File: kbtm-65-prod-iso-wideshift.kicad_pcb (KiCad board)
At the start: 2 copper layers, 302.2 x 93.5 mm, 170 parts, among them J1 TYPE-C-31-M12_13_EDITED, J2 AVR-ISP-6, SW1 SW_Push, U1 ATmega32U4-AU, U2 WE-TVS-82400102, Y1 Crystal_GND24_Small

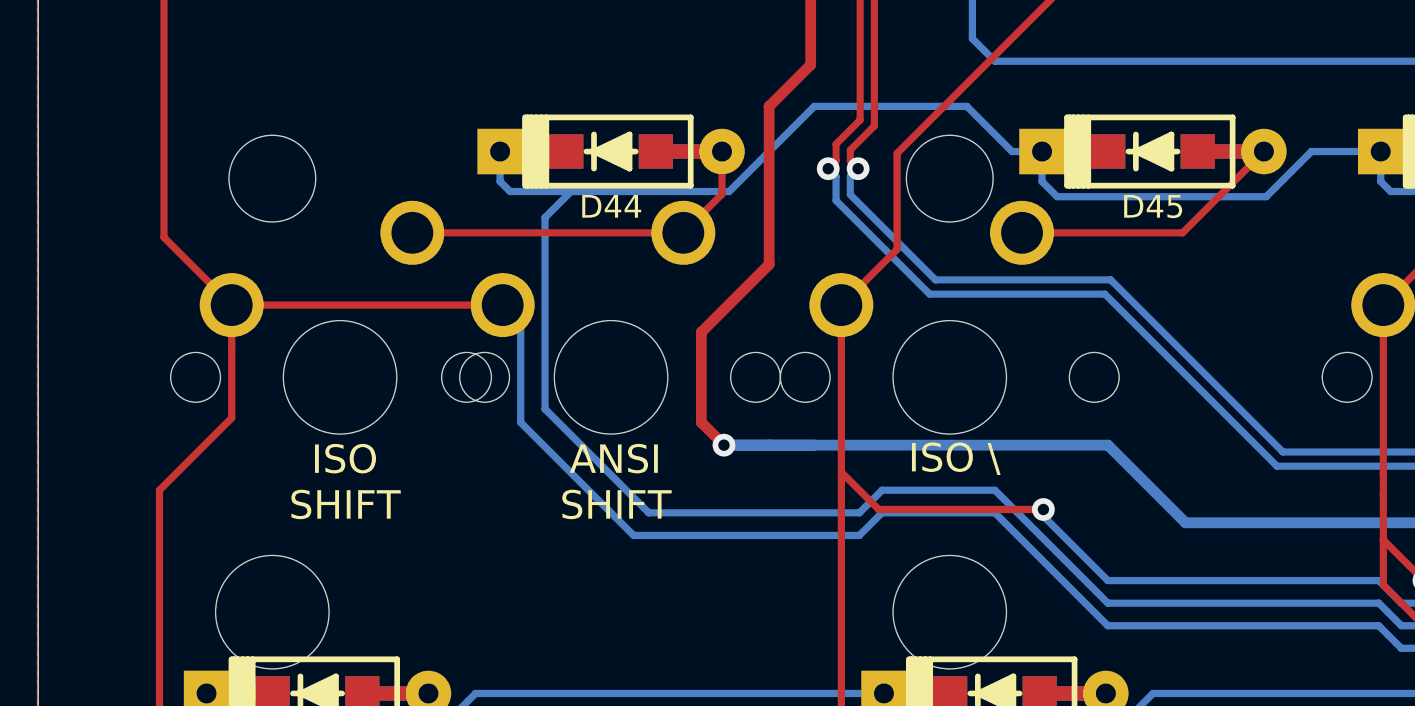
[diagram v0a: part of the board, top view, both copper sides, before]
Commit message: final prod version with all keys and fills filled in
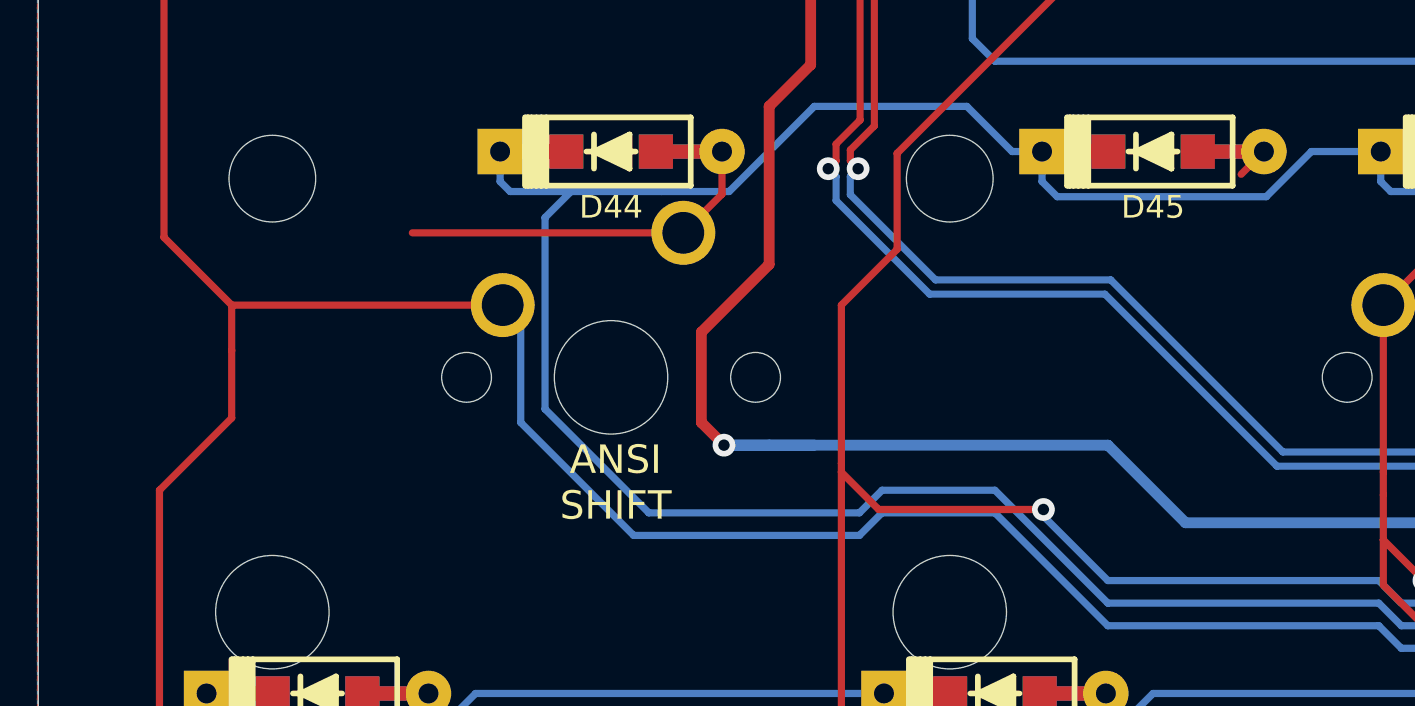
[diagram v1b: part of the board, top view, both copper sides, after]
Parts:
- removed MX_1.25U_L_SHIFT1: MX-NoLED, mini-MX-Tweaks:MXOnly-1.25U-NoLED_tweak
- removed MX_L_BSLASH1: MX-NoLED, mini-MX-Tweaks:MXOnly-1U-NoLED_tweak
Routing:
- net Net-(D45-Pad2): track 9.69 -> 1.13 mm
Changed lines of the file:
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@@
   )
   (footprint "mini-MX-Tweaks:MXOnly-1.25U-NoLED_tweak" (layer "F.Cu")
-    (at 24.60625 81.75625)
-    (attr through_hole)
-    (fp_text reference "MX_1.25U_L_SHIFT1" (at 0 3.175) (layer "Dwgs.User")
-        (effects (font (size 1 1) (thickness 0.15)))
-    )
-    (fp_text value "MX-NoLED" (at 0 -7.9375) (layer "Dwgs.User")
-        (effects (font (size 1 1) (thickness 0.15)))
-    )
-    (fp_line (start -11.90625 -9.525) (end 11.90625 -9.525)
-      (stroke (width 0.15) (type solid)) (layer "Dwgs.User"))
-    (fp_line (start -11.90625 9.525) (end -11.90625 -9.525)
-      (stroke (width 0.15) (type solid)) (layer "Dwgs.User"))
-    (fp_line (start -11.90625 9.525) (end 11.90625 9.525)
-      (stroke (width 0.15) (type solid)) (layer "Dwgs.User"))
-    (fp_line (start -7 -7) (end -7 -5)
-      (stroke (width 0.15) (type solid)) (layer "Dwgs.User"))
-    (fp_line (start -7 5) (end -7 7)
-      (stroke (width 0.15) (type solid)) (layer "Dwgs.User"))
-    (fp_line (start -7 7) (end -5 7)
-      (stroke (width 0.15) (type solid)) (layer "Dwgs.User"))
-    (fp_line (start -5 -7) (end -7 -7)
-      (stroke (width 0.15) (type solid)) (layer "Dwgs.User"))
-    (fp_line (start 5 -7) (end 7 -7)
-      (stroke (width 0.15) (type solid)) (layer "Dwgs.User"))
-    (fp_line (start 5 7) (end 7 7)
-      (stroke (width 0.15) (type solid)) (layer "Dwgs.User"))
-    (fp_line (start 7 -7) (end 7 -5)
-      (stroke (width 0.15) (type solid)) (layer "Dwgs.User"))
-    (fp_line (start 7 7) (end 7 5)
-      (stroke (width 0.15) (type solid)) (layer "Dwgs.User"))
-    (fp_line (start 11.90625 -9.525) (end 11.90625 9.525)
-      (stroke (width 0.15) (type solid)) (layer "Dwgs.User"))
-    (pad "" np_thru_hole circle (at -5.08 0 48.0996) (size 1.75 1.75) (drill 1.75) (layers "*.Cu" "*.Mask"))
-    (pad "" np_thru_hole circle (at 0 0) (size 3.9878 3.9878) (drill 3.9878) (layers "*.Cu" "*.Mask"))
-    (pad "" np_thru_hole circle (at 5.08 0 48.0996) (size 1.75 1.75) (drill 1.75) (layers "*.Cu" "*.Mask"))
-    (pad "1" thru_hole circle (at -3.81 -2.54) (size 2.25 2.25) (drill 1.47) (layers "*.Cu" "*.Mask")
-      (net 92 "COL0"))
-    (pad "2" thru_hole circle (at 2.54 -5.08) (size 2.25 2.25) (drill 1.47) (layers "*.Cu" "*.Mask")
-      (net 101 "Net-(D44-Pad2)"))
-  )
-  (footprint "mini-MX-Tweaks:MXOnly-1.25U-NoLED_tweak" (layer "F.Cu")
     (at 48.41875 100.80625)
     (attr through_hole)
@@
       (net 101 "Net-(D44-Pad2)"))
   )
-  (footprint "mini-MX-Tweaks:MXOnly-1U-NoLED_tweak" locked (layer "F.Cu")
-    (at 46.0375 81.75625)
-    (attr through_hole)
-    (fp_text reference "MX_L_BSLASH1" (at 0 3.175) (layer "Dwgs.User")
-        (effects (font (size 1 1) (thickness 0.15)))
-    )
-    (fp_text value "MX-NoLED" (at 0 -7.9375) (layer "Dwgs.User")
-        (effects (font (size 1 1) (thickness 0.15)))
-    )
-    (fp_line (start -9.525 -9.525) (end 9.525 -9.525)
-      (stroke (width 0.15) (type solid)) (layer "Dwgs.User"))
-    (fp_line (start -9.525 9.525) (end -9.525 -9.525)
-      (stroke (width 0.15) (type solid)) (layer "Dwgs.User"))
-    (fp_line (start -7 -7) (end -7 -5)
-      (stroke (width 0.15) (type solid)) (layer "Dwgs.User"))
-    (fp_line (start -7 5) (end -7 7)
-      (stroke (width 0.15) (type solid)) (layer "Dwgs.User"))
-    (fp_line (start -7 7) (end -5 7)
-      (stroke (width 0.15) (type solid)) (layer "Dwgs.User"))
-    (fp_line (start -5 -7) (end -7 -7)
-      (stroke (width 0.15) (type solid)) (layer "Dwgs.User"))
-    (fp_line (start 5 -7) (end 7 -7)
-      (stroke (width 0.15) (type solid)) (layer "Dwgs.User"))
-    (fp_line (start 5 7) (end 7 7)
-      (stroke (width 0.15) (type solid)) (layer "Dwgs.User"))
-    (fp_line (start 7 -7) (end 7 -5)
-      (stroke (width 0.15) (type solid)) (layer "Dwgs.User"))
-    (fp_line (start 7 7) (end 7 5)
-      (stroke (width 0.15) (type solid)) (layer "Dwgs.User"))
-    (fp_line (start 9.525 -9.525) (end 9.525 9.525)
-      (stroke (width 0.15) (type solid)) (layer "Dwgs.User"))
-    (fp_line (start 9.525 9.525) (end -9.525 9.525)
-      (stroke (width 0.15) (type solid)) (layer "Dwgs.User"))
-    (pad "" np_thru_hole circle locked (at -5.08 0 48.0996) (size 1.75 1.75) (drill 1.75) (layers "*.Cu" "*.Mask"))
-    (pad "" np_thru_hole circle locked (at 0 0) (size 3.9878 3.9878) (drill 3.9878) (layers "*.Cu" "*.Mask"))
-    (pad "" np_thru_hole circle locked (at 5.08 0 48.0996) (size 1.75 1.75) (drill 1.75) (layers "*.Cu" "*.Mask"))
-    (pad "1" thru_hole circle locked (at -3.81 -2.54) (size 2.25 2.25) (drill 1.47) (layers "*.Cu" "*.Mask")
-      (net 82 "COL1"))
-    (pad "2" thru_hole circle locked (at 2.54 -5.08) (size 2.25 2.25) (drill 1.47) (layers "*.Cu" "*.Mask")
-      (net 49 "Net-(D45-Pad2)"))
-  )
   (footprint "mini-general-tweaks:D_SOD123_axial-dual" (layer "F.Cu")
     (at 298.67225 32.54375)
@@
     (effects (font (size 1 1) (thickness 0.15)) (justify mirror))
   )
-  (gr_text "ISO\nSHIFT" (at 24.76784 85.45579) (layer "F.SilkS")
-    (effects (font (size 1 1) (thickness 0.15)))
-  )
   (gr_text "STEPPED\nCAPS" (at 22.21484 66.51879) (layer "F.SilkS")
     (effects (font (size 1 1) (thickness 0.15)))
@@
     (effects (font (size 1 1) (thickness 0.15)))
   )
-  (gr_text "ISO \\" (at 46.2 84.6) (layer "F.SilkS")
-    (effects (font (size 1 1) (thickness 0.15)))
-  )
   (gr_text "Licensed under CERN-OHL-S v2" (at 112.7125 107.95) (layer "F.SilkS")
     (effects (font (size 1.3 1.3) (thickness 0.2)))
@@
   (segment (start 310.515 57.62625) (end 307.90625 55.0175) (width 0.254) (layer "F.Cu") (net 48))
   (segment (start 56.281251 74.618749) (end 57.08125 73.81875) (width 0.254) (layer "F.Cu") (net 49))
-  (segment (start 54.22375 76.67625) (end 56.281251 74.618749) (width 0.254) (layer "F.Cu") (net 49))
-  (segment (start 48.5775 76.67625) (end 54.22375 76.67625) (width 0.254) (layer "F.Cu") (net 49))
   (segment (start 67.6275 76.67625) (end 68.9875 75.31625) (width 0.254) (layer "F.Cu") (net 50))
   (segment (start 68.9875 75.31625) (end 68.9875 73.81875) (width 0.254) (layer "F.Cu") (net 50))
